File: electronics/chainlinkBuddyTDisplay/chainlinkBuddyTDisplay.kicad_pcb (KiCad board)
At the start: 2 copper layers, 74.9 x 49.5 mm, 12 parts, among them J1 Output, J2 Screw_Terminal_01x03, J3 Barrel_Jack_Switch, U1 TTGO_TDisplay, U2 LM7805_TO220

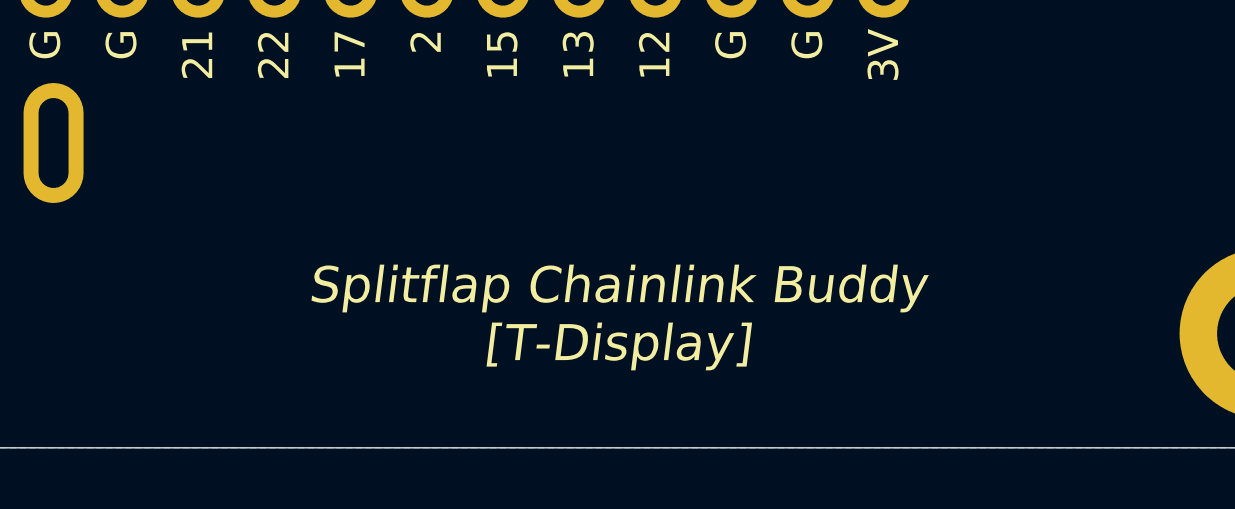
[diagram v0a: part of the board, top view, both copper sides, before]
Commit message: Add version numbers to chainlink PCBs
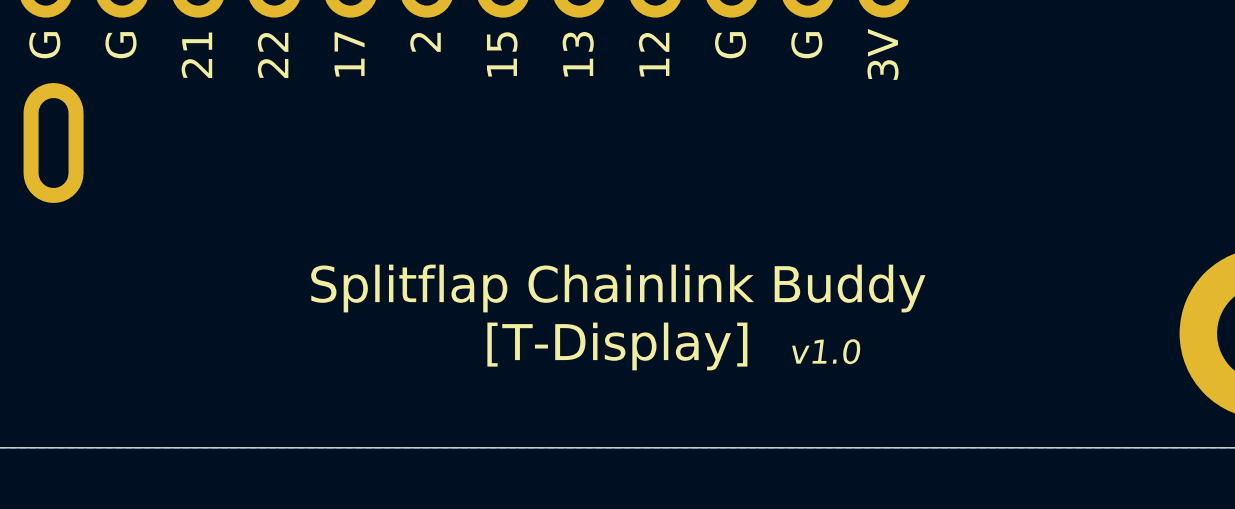
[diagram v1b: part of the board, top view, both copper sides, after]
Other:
- board text added: "v1.0"

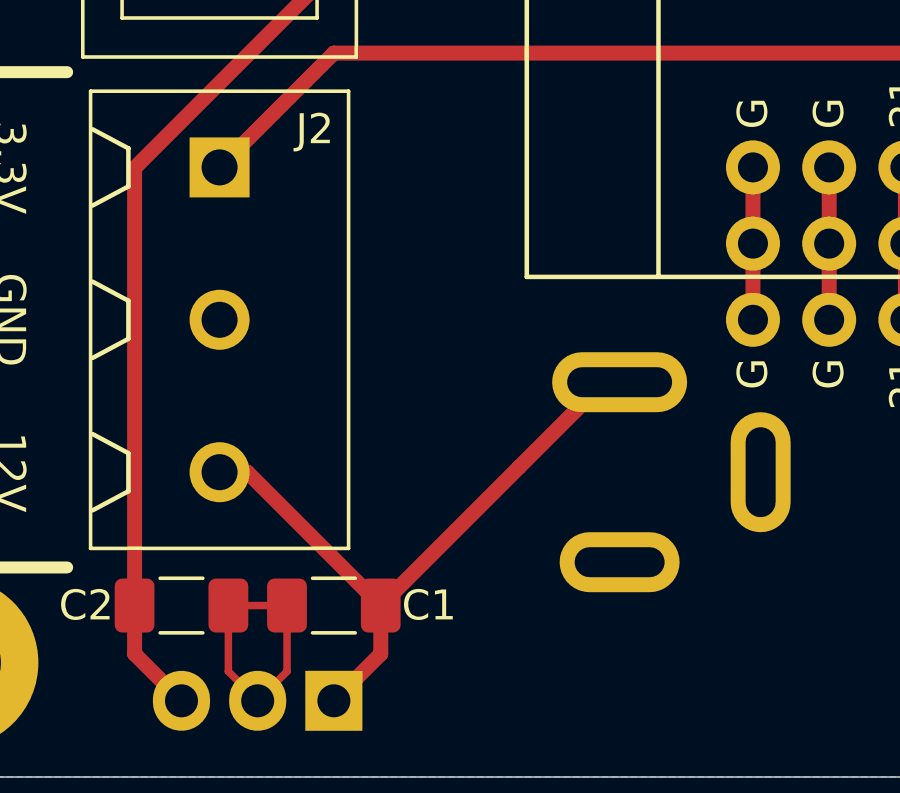
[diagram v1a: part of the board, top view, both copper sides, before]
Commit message: Add spare 12V pins to Chainlink Buddy T-Display
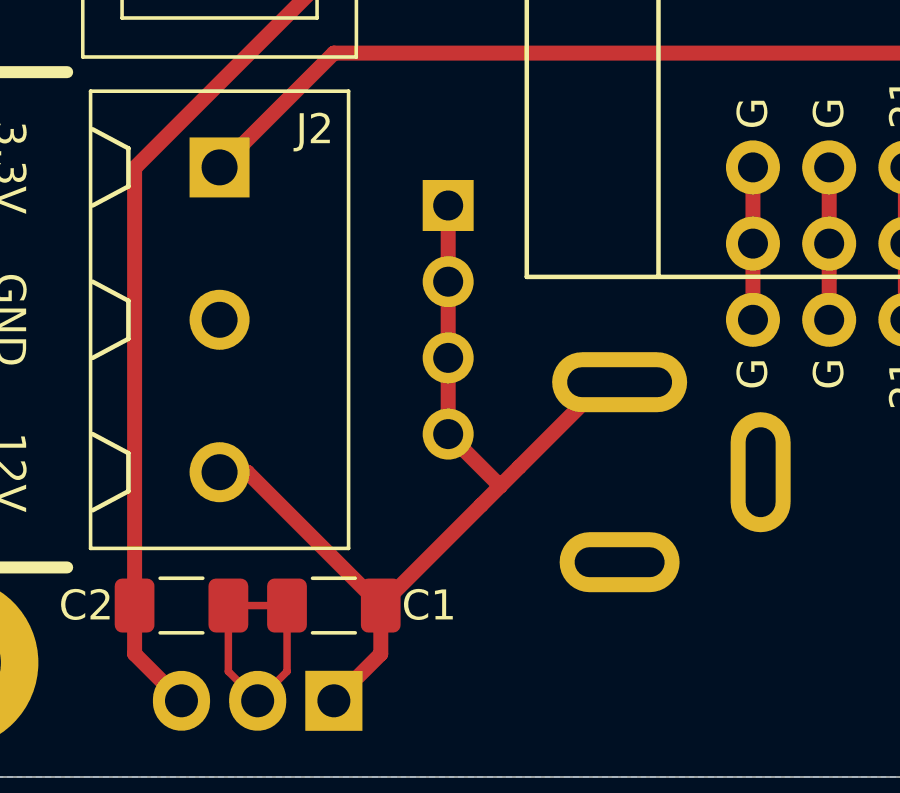
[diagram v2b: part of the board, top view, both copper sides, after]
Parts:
- added J7: Conn_01x04, ModifiedSymbols:PinHoles_1x04_P2.54mm_NoSilk, F.Cu at (83.8, 94.0)
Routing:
- net +12V: track 22.1 -> 32.2 mm
